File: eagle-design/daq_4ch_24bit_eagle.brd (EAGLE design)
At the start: 100 x 100 mm, 175 parts, among them J1 B6252HB-NPP3G-50, J2 B6252HB-NPP3G-50, J3 USB, J4 B6252HB-NPP3G-50, J5 B6252HB-NPP3G-50, J6 B6252HB-NPP3G-50, J7 B6252HB-NPP3G-50, U1 TS5A3359DCU, U10 74LVC1G3157, U11 ADS122U04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

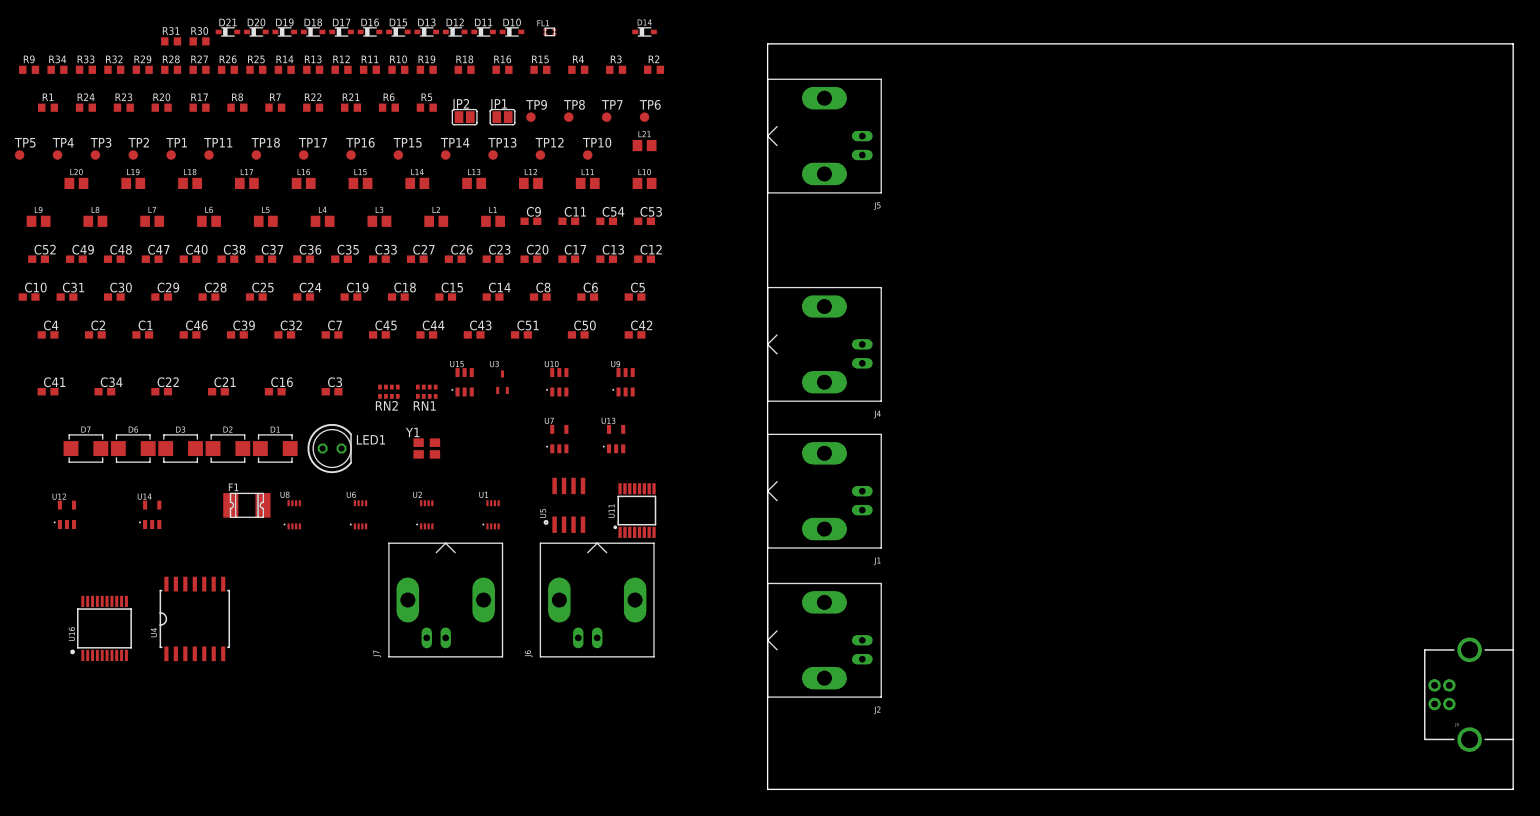
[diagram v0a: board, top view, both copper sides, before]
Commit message: Fixes to schematic and library, begin placement and routing
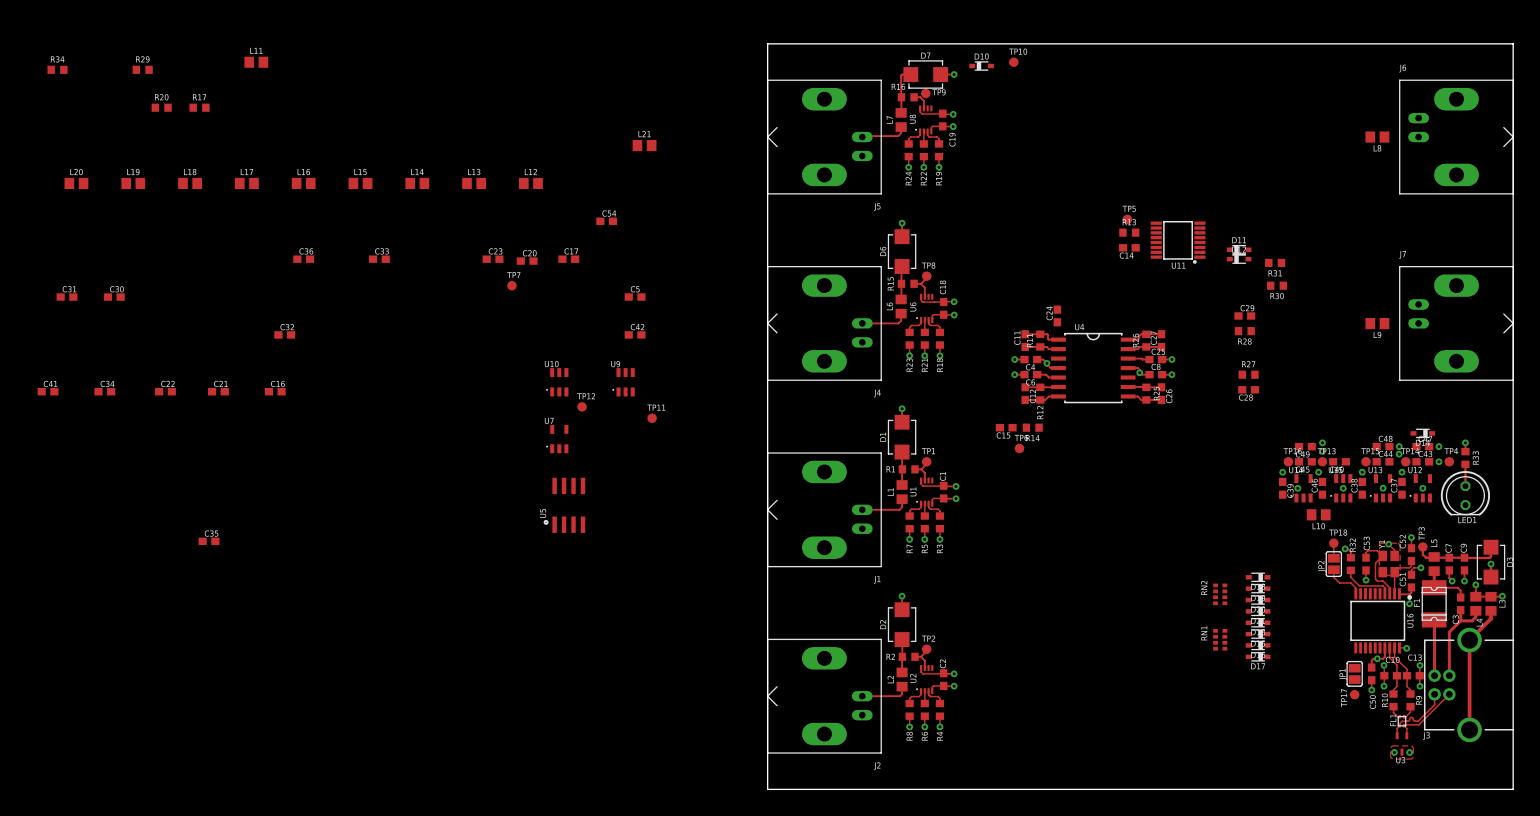
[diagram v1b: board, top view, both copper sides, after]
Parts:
- LED1: value (none) -> GREEN
- R30, R31: value (none) -> 10k
- moved R9 203.7 mm to (86.2, 11.9), turned to 90 degrees
- moved R33 192.2 mm to (93.6, 44.5), turned to 90 degrees
- moved TP4 191.2 mm to (91.4, 43.9)
- moved C10 189.6 mm to (83.6, 15.2), turned to 180 degrees
- moved C52 188.4 mm to (86.4, 31.5), turned to 90 degrees
- moved TP3 185.7 mm to (87.9, 32.5), turned to 90 degrees
- moved U12 181.9 mm to (87.9, 40.4)
- moved L9 180.1 mm to (81.8, 62.5), turned to 180 degrees
- moved R32 178.6 mm to (78.2, 30.2), turned to 90 degrees
- moved D3 176.4 mm to (97.0, 30.5), turned to 270 degrees
- moved L8 172.3 mm to (81.8, 87.5), turned to 180 degrees
- moved C47 172.3 mm to (87.9, 46.0)
- moved C48 172.0 mm to (82.5, 46.0)
- moved U16 170.7 mm to (81.8, 22.6), turned to 180 degrees
- moved C49 166.8 mm to (72.1, 46.0), turned to 180 degrees
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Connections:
- net N$27 renamed USBGND
- net N$28 renamed VUSB
- net N$32 renamed USBD_P
- net N$33 renamed USBD_N
- net USB-D+ renamed USB-D_P
- net USB-D- renamed USB-D_N
- removed net N$16: D15.A, RN1.7
- removed net N$17: D16.A, RN1.6
- removed net N$18: D17.A, RN1.5
- removed net N$19: D13.A, RN1.8
- removed net V+: U8.8
- net ADC_CH2: no longer U10.4
- net ADC_CH3: now also U10.4
- net CH0_SW1: now also D13.A, RN1.8
- net CH0_SW2: now also D15.A, RN1.7
- net CH1_SW1: now also D16.A, RN1.6
- net CH1_SW2: now also D17.A, RN1.5
- net GND: now also TP4.TP, Y1.2; no longer TP2.TP, U8.4, Y1.3
- net N$40: now also Y1.1; no longer Y1.2
- net N$41: now also Y1.3; no longer Y1.1
- net N$48: now also TP1.TP; no longer TP3.TP
- net N$71: now also TP2.TP; no longer TP4.TP
- net VAA: now also U8.8
- net VBUS: now also TP3.TP; no longer TP1.TP
- net VSS: now also U8.4
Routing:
- net GND: track 0.00 -> 54.9 mm, vias 0 -> 51
- net VAA: track 0.00 -> 24.0 mm, vias 0 -> 5
- net VSS: track 0.00 -> 17.9 mm, vias 0 -> 5
- net N$29: track 0.00 -> 17.2 mm
- net USBGND: track 0.00 -> 12.5 mm
- net VBUS: track 0.00 -> 11.8 mm
- net VDD: track 0.00 -> 10.7 mm, vias 0 -> 4
- net N$41: track 0.00 -> 10.0 mm
- net USBD_N: track 0.00 -> 9.30 mm
- net USBD_P: track 0.00 -> 9.30 mm
- net VUSB: track 0.00 -> 7.50 mm
- net USB-D_P: track 0.00 -> 7.08 mm
- net N$20: track 0.00 -> 6.88 mm
- net N$26: track 0.00 -> 6.87 mm
- net N$71: track 0.00 -> 6.86 mm
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- added copper zone on layer 1, net GND
- added copper zone on layer 2, net GND

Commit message: Fix on schematic, placement and routing done, needs impendance calculation, first iteration - could be improved
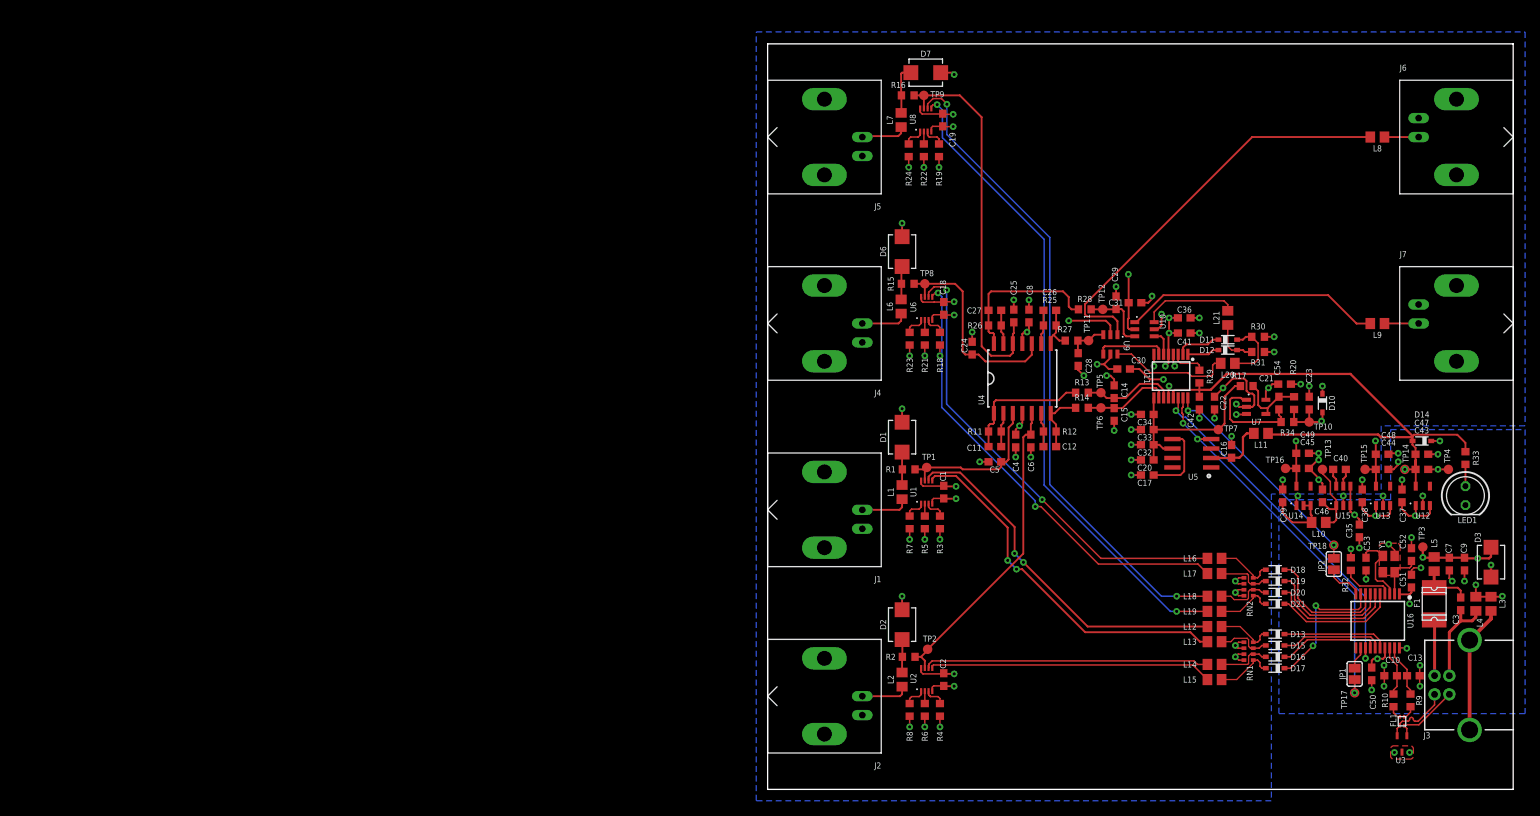
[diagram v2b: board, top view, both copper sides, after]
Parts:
- moved R34 171.6 mm to (69.7, 49.3)
- moved R20 157.0 mm to (70.6, 51.8), turned to 270 degrees
- moved L20 156.3 mm to (61.7, 57.1), turned to 180 degrees
- moved L19 156.0 mm to (59.9, 23.9), turned to 180 degrees
- moved C35 154.3 mm to (79.4, 34.7), turned to 270 degrees
- moved C41 152.6 mm to (55.9, 61.2), turned to 180 degrees
- moved L18 148.2 mm to (59.9, 25.9), turned to 180 degrees
- moved R29 147.6 mm to (57.9, 55.4), turned to 270 degrees
- moved R17 145.3 mm to (64.3, 54.1)
- moved L11 143.6 mm to (66.2, 47.8)
- moved C31 143.3 mm to (49.3, 65.3), turned to 180 degrees
- moved C21 143.0 mm to (69.3, 54.4)
- moved C22 140.7 mm to (59.9, 51.8), turned to 270 degrees
- moved L17 139.9 mm to (59.9, 29.0), turned to 180 degrees
- moved C34 139.9 mm to (50.9, 50.3), turned to 180 degrees
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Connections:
- removed net VREF: C20.1, R17.1, TP7.TP, U5.6
- net CH2_SW3: no longer L21.1
- net CH3_SW3: now also L21.1
- net VAA: now also U7.5
- net VDD: no longer U7.5
- net V_REF: now also C20.1, R17.1, TP7.TP, U5.6
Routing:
- net N$80: track 0.00 -> 87.9 mm, vias 0 -> 2
- net N$79: track 0.00 -> 87.0 mm, vias 0 -> 2
- net VDD: track 10.7 -> 87.5 mm
- net N$55: track 0.00 -> 62.4 mm, vias 0 -> 2
- net N$54: track 0.00 -> 62.0 mm, vias 0 -> 2
- net N$65: track 0.00 -> 55.5 mm
- net VSS: track 17.9 -> 71.0 mm, vias 5 -> 17
- net N$15: track 0.00 -> 51.0 mm, vias 0 -> 2
- net N$46: track 0.00 -> 49.1 mm, vias 0 -> 2
- net N$47: track 0.00 -> 48.8 mm, vias 0 -> 2
- net GND: track 54.9 -> 102.8 mm, vias 51 -> 70
- net N$23: track 0.00 -> 47.3 mm, vias 0 -> 2
- net N$81: track 5.44 -> 51.8 mm
- net N$70: track 0.00 -> 38.3 mm
- net N$69: track 0.00 -> 38.0 mm
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- added copper zone on layer 16, net VAA
- added copper zone on layer 15, net VBUS
- added copper zone on layer 16, net VDD
- added copper zone on layer 15, net VSS
- added copper zone on layer 15, net VSSA
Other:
- board text added: "A little schematic adjustment to straighten the design here is needed"
